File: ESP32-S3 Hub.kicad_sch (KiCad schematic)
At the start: 23 parts, among them U1 ESP32-S3, Y1 ABM11-40.000MHZ-B1U-T3, 10ppm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

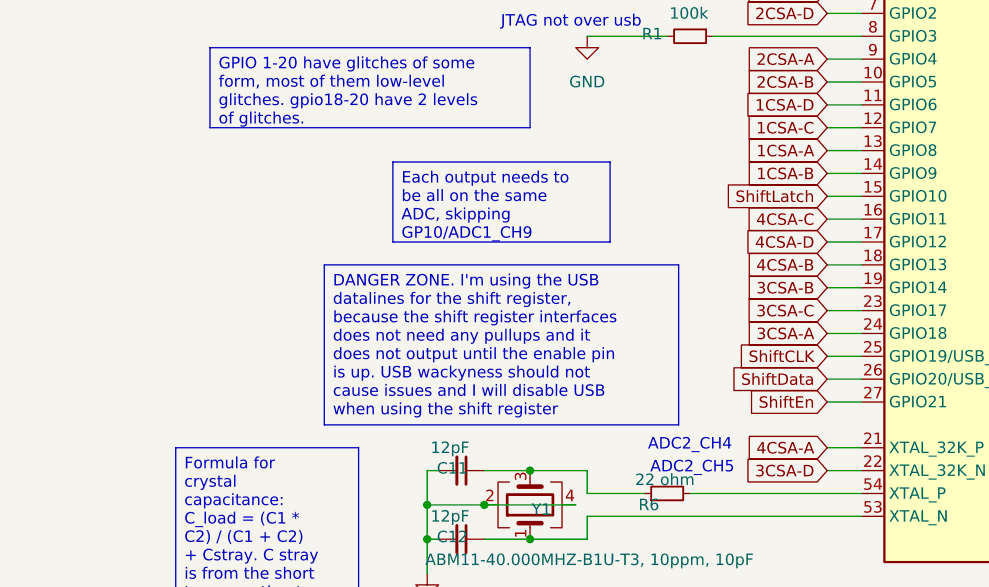
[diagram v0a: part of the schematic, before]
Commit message: Replaced LED driver with 2 shift registers
My initial approach from the first version was better design, I need 80+ mhz to get adequate PWM signals.
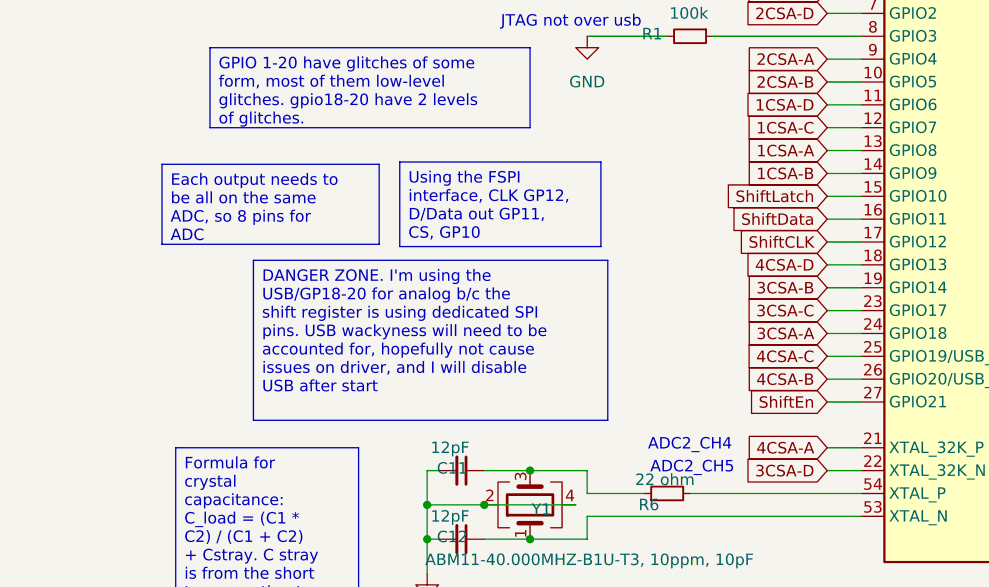
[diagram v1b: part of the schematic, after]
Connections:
- net 4CSA-B: now also U1.26 (GPIO20/USB_D+); no longer U1.18 (GPIO13)
- net 4CSA-C: now also U1.25 (GPIO19/USB_D-); no longer U1.16 (GPIO11)
- net 4CSA-D: now also U1.18 (GPIO13); no longer U1.17 (GPIO12)
- net ShiftCLK: now also U1.17 (GPIO12); no longer U1.25 (GPIO19/USB_D-)
- net ShiftData: now also U1.16 (GPIO11); no longer U1.26 (GPIO20/USB_D+)
